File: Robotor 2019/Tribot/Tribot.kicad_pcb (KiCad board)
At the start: 2 copper layers, 95.2 x 95.2 mm, 74 parts, among them J1 Conn_01x03_Male, J2 Conn_01x04_Female, J3 USB_B_Mini, J4 Conn_01x04_Female, J5 Conn_01x04_Female, J6 Conn_01x04_Female, J7 Conn_01x03_Female, J8 Conn_01x03_Female, M1 Motor_DC, M2 Motor_DC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

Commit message: The PCB for Tribot up to the point we realised we need a 2nd floor.
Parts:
- removed J4: Conn_01x04_Female, Connector_PinHeader_2.54mm:PinHeader_1x04_P2.54mm_Vertical
- removed the R8 at (139.3, 20.0)
- removed the R8 at (136.6, 82.4)
- added R8: 10K, Resistor_SMD:R_0805_2012Metric_Pad1.15x1.40mm_HandSolder, F.Cu at (228.8, 101.6)
- C4, C5, C6, C7, J3, R10, R11, R3, R9, Y1, Y2: moved to B.Cu
- moved J3 166.6 mm to (263.5, 85.7), turned to 270 degrees
- moved J2 161.8 mm to (237.5, 125.7), turned to 0 degrees
- moved C3 150.6 mm to (38.3, 156.2)
- moved J8 142.1 mm to (251.8, 126.4)
- moved J7 142.1 mm to (256.5, 126.4)
- moved Y2 133.6 mm to (215.4, 66.0), turned to 180 degrees
- moved Y1 128.2 mm to (233.2, 66.0)
- moved R7 128.0 mm to (261.9, 128.3)
- moved JP2 127.3 mm to (229.9, 105.4), turned to 270 degrees
- moved R5 122.8 mm to (246.6, 128.3)
- moved C8 122.4 mm to (38.3, 162.6)
- moved JP1 122.3 mm to (227.3, 109.2), turned to 90 degrees
- moved R11 121.2 mm to (253.0, 89.5)
- moved CP5 113.7 mm to (61.7, 179.1)
- moved C5 112.9 mm to (227.1, 71.1), turned to 180 degrees
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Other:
- outline, holes or cut-outs redrawn

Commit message: Bottom tribot circuit board.
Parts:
- removed C12: 100n, Capacitor_SMD:C_0805_2012Metric_Pad1.15x1.40mm_HandSolder
- removed CP1: 1uF, Capacitor_SMD:CP_Elec_4x5.3
- removed J6: Conn_01x04_Female, Connector_PinHeader_2.54mm:PinHeader_1x04_P2.54mm_Vertical
- removed U2: AMS1117-3V3, Package_TO_SOT_SMD:SOT-223-3_TabPin2
- added BOOT_PIN1: Conn_01x02, Connector_PinHeader_2.54mm:PinHeader_1x02_P2.54mm_Vertical, F.Cu at (199.9, 52.1)
- added BOOT_PIN2: Conn_01x02, Connector_PinHeader_2.54mm:PinHeader_1x02_P2.54mm_Vertical, F.Cu at (73.4, 117.3)
- added J4: Conn_01x04_Female, Connector_PinHeader_2.54mm:PinHeader_1x04_P2.54mm_Vertical, F.Cu at (52.1, 60.3)
- added M_PIN1: Conn_01x03, Connector_PinSocket_2.54mm:PinSocket_1x03_P2.54mm_Vertical, F.Cu at (111.5, 143.6)
- added M_PIN2: Conn_01x03, Connector_PinSocket_2.54mm:PinSocket_1x03_P2.54mm_Vertical, F.Cu at (238.0, 80.8)
- added M_PIN3: Conn_01x03, Connector_PinSocket_2.54mm:PinSocket_1x03_P2.54mm_Vertical, F.Cu at (116.8, 143.5)
- added M_PIN4: Conn_01x03, Connector_PinSocket_2.54mm:PinSocket_1x03_P2.54mm_Vertical, F.Cu at (243.3, 80.8)
- added PRGRM_PIN1: Conn_01x02, Connector_PinHeader_2.54mm:PinHeader_1x02_P2.54mm_Vertical, F.Cu at (192.8, 39.9)
- added PRGRM_PIN2: Conn_01x02, Connector_PinHeader_2.54mm:PinHeader_1x02_P2.54mm_Vertical, F.Cu at (66.3, 102.6)
- added USB_PIN1: Conn_01x02, Connector_PinHeader_2.54mm:PinHeader_1x02_P2.54mm_Vertical, F.Cu at (68.8, 107.7)
- added USB_PIN2: Conn_01x02, Connector_PinHeader_2.54mm:PinHeader_1x02_P2.54mm_Vertical, F.Cu at (195.3, 45.0)
- added US_PIN1: Conn_01x02, Connector_PinHeader_2.54mm:PinHeader_1x02_P2.54mm_Vertical, F.Cu at (69.6, 122.9)
- added US_PIN2: Conn_01x02, Connector_PinHeader_2.54mm:PinHeader_1x02_P2.54mm_Vertical, F.Cu at (196.1, 60.2)
- added US_PIN3: Conn_01x02, Connector_PinHeader_2.54mm:PinHeader_1x02_P2.54mm_Vertical, F.Cu at (196.1, 52.1)
- added US_PIN4: Conn_01x02, Connector_PinHeader_2.54mm:PinHeader_1x02_P2.54mm_Vertical, F.Cu at (69.6, 114.8)
- added V_PIN1: Conn_01x02, Connector_Wire:SolderWirePad_1x02_P5.08mm_Drill1.5mm, F.Cu at (66.5, 148.6)
- added V_PIN2: Conn_01x03, Connector_Wire:SolderWirePad_1x03_P5.715mm_Drill2mm, F.Cu at (48.5, 37.3)
- added V_PIN2: Conn_01x02, Connector_Wire:SolderWirePad_1x02_P5.08mm_Drill1.5mm, F.Cu at (193.0, 85.9)
- D1, D2, D3, D4, D5, D6, D7, D8: footprint Diode_THT:D_DO-15_P5.08mm_Vertical_AnodeUp -> Diode_THT:D_A-405_P5.08mm_Vertical_AnodeUp
- J3, R10, R11, R3, R9: moved to F.Cu
- moved J2 200.9 mm to (47.5, 60.3)
- moved J7 185.7 mm to (93.7, 37.0)
- moved R2 182.9 mm to (46.0, 135.9), turned to 90 degrees
- moved U4 179.3 mm to (52.1, 128.3), turned to 90 degrees
- moved J8 176.7 mm to (100.3, 35.3)
- moved C1 169.8 mm to (46.7, 145.3)
- moved R1 168.1 mm to (46.7, 142.7)
- moved CP6 168.0 mm to (82.5, 13.7), turned to 270 degrees
- moved R7 167.6 mm to (107.3, 63.6)
- moved CP4 166.6 mm to (53.3, 148.6)
- moved C8 163.8 mm to (82.5, 4.83), turned to 90 degrees
- moved R5 162.9 mm to (94.4, 70.4)
- moved R6 161.7 mm to (53.3, 144.8), turned to 180 degrees
- moved U5 161.6 mm to (58.4, 158.8)
- moved R12 161.5 mm to (58.4, 166.4)
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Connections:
- C15 pad 1: +5V -> 5V
- C17 pad 1: +5V -> 5V
- C18 pad 1: +5V -> 5V
- C21 pad 1: +5V -> 5V
- C8 pad 1: +7.5V -> EXT_VCC
- CP2 pad 1: +7.5V -> EXT_VCC
- CP3 pad 1: +7.5V -> EXT_VCC
- CP4 pad 1: +3V3 -> 3V3
- CP6 pad 1: +7.5V -> EXT_VCC
- D1 pad 1: +7.5V -> EXT_VCC
- D3 pad 1: +7.5V -> EXT_VCC
- D5 pad 1: +7.5V -> EXT_VCC
- D7 pad 1: +7.5V -> EXT_VCC
- J1 pad 1: +7.5V -> EXT_VCC
- J7 pad 3: +3V3 -> 3V3
- J8 pad 3: +3V3 -> 3V3
- R1 pad 1: +3V3 -> 3V3
- R10 pad 1: PA12 -> USB++
- R12 pad 1: +5V -> 5V
- R14 pad 1: +5V -> 5V
- R16 pad 1: +5V -> 5V
- R18 pad 1: +5V -> 5V
- R2 pad 1: +3V3 -> 3V3
- R5 pad 1: +3V3 -> 3V3
- R6 pad 1: +3V3 -> 3V3
- R7 pad 1: +3V3 -> 3V3
- R9 pad 2: PA11 -> USB--
- U1 pad 3: +7.5V -> EXT_VCC
- U3 pad 3: +7.5V -> EXT_VCC
- U4 pad 18: EnA -> EnA_B
- U4 pad 19: EnB -> EnB_B
- U4 pad 20: BOOT1 -> BOOT1_B
- U4 pad 24: +3V3 -> 3V3
- U4 pad 25: US1_IN -> US1P_IN
- U4 pad 26: US1_OUT -> US1P_OUT
- U4 pad 27: US2_IN -> US2P_IN
- U4 pad 28: US2_OUT -> US2P_OUT
- U4 pad 32: PA11 -> USB-
- U4 pad 33: PA12 -> USB+
- U4 pad 34: DIO -> DIO_B
- U4 pad 36: +3V3 -> 3V3
- U4 pad 37: CLK -> CLK_B
- U4 pad 38: M2IN2 -> M2IN2_B
- U4 pad 39: M2IN1 -> M2IN1_B
- U4 pad 40: M1IN2 -> M1IN2_B
- U4 pad 41: M1IN1 -> M1IN1_B
- U4 pad 44: BOOT0 -> BOOT0_B
- U4 pad 45: US3_IN -> Net-(U4-Pad45)
- U4 pad 46: US3_OUT -> Net-(U4-Pad46)
- U4 pad 48: +3V3 -> 3V3
- U6 pad 6: +7.5V -> EXT_VCC
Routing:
- net M2IN1_B: track 0.00 -> 131.5 mm
- net M2IN2_B: track 0.00 -> 129.9 mm
- net OSC32-IN: track 0.00 -> 118.9 mm, vias 0 -> 1
- net M1IN2_B: track 0.00 -> 118.1 mm
- net M1IN1_B: track 0.00 -> 113.6 mm
- net 5V: track 0.00 -> 104.7 mm, vias 0 -> 1
- net OSC-OUT: track 0.00 -> 90.3 mm, vias 0 -> 1
- net OSC32-OUT: track 0.00 -> 86.5 mm, vias 0 -> 1
- net 3V3: track 0.00 -> 81.3 mm, vias 0 -> 3
- net OSC-IN: track 0.00 -> 74.6 mm, vias 0 -> 1
- net EnB_B: track 0.00 -> 70.3 mm
- net EnA_B: track 0.00 -> 66.6 mm
- net BOOT0_B: track 0.00 -> 46.6 mm, vias 0 -> 1
- net CLK_B: track 0.00 -> 34.4 mm
- net DIO_B: track 0.00 -> 33.9 mm
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- added copper zone on B.Cu, net GND
- added copper zone on F.Cu, net GND
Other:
- board size 95.2 x 95.2 mm -> 220.5 x 156.7 mm

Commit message: Tribot bottom circuit board final version (hopefully)
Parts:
- added D10: DIODE, Diode_THT:D_A-405_P5.08mm_Vertical_AnodeUp, F.Cu at (62.0, 48.3)
- added REF**: MountingHole_2.5mm, MountingHole:MountingHole_2.5mm, F.Cu at (127.5, 130.6)
- added REF**: MountingHole_2.5mm, MountingHole:MountingHole_2.5mm, F.Cu at (127.5, 145.5)
- added REF**: MountingHole_2.5mm, MountingHole:MountingHole_2.5mm, F.Cu at (45.7, 145.8)
- added REF**: MountingHole_2.5mm, MountingHole:MountingHole_2.5mm, F.Cu at (45.7, 130.8)
- moved C5 12.4 mm to (119.1, 144.8)
- moved C6 12.4 mm to (109.5, 144.8)
- moved C7 12.4 mm to (109.0, 124.5)
- moved Y1 12.4 mm to (119.1, 134.6)
- moved Y2 12.4 mm to (110.5, 134.6)
- moved C4 11.7 mm to (117.1, 123.2), turned to 90 degrees
- moved M_PIN3 10.9 mm to (122.7, 152.7)
- moved M_PIN2 10.9 mm to (243.8, 89.9)
- moved M_PIN4 10.9 mm to (249.2, 89.9)
- moved M_PIN1 10.9 mm to (117.3, 152.7)
- moved R15 8.38 mm to (66.8, 144.8)
- moved U7 7.94 mm to (59.9, 145.0)
- moved R14 7.94 mm to (59.9, 152.7)
- moved C17 7.94 mm to (66.3, 148.8)
- moved C18 7.58 mm to (65.8, 134.1)
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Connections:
- C8 pad 1: EXT_VCC -> +7.5V
- CP2 pad 1: EXT_VCC -> +7.5V
- CP3 pad 1: EXT_VCC -> +7.5V
- CP6 pad 1: EXT_VCC -> +7.5V
- D1 pad 1: EXT_VCC -> +7.5V
- D3 pad 1: EXT_VCC -> +7.5V
- D5 pad 1: EXT_VCC -> +7.5V
- D7 pad 1: EXT_VCC -> +7.5V
- J1 pad 1: EXT_VCC -> +7.5V
- U1 pad 3: EXT_VCC -> +7.5V
- U3 pad 3: EXT_VCC -> +7.5V
- U6 pad 6: EXT_VCC -> +7.5V
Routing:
- net M2IN2_B: track 129.9 -> 155.7 mm
- net M2IN1_B: track 131.5 -> 155.6 mm
- net M1IN2_B: track 118.1 -> 139.7 mm
- net M1IN1_B: track 113.6 -> 135.1 mm
- net 5V: track 104.7 -> 87.9 mm
- net OSC-OUT: track 90.3 -> 75.2 mm
- net EnB_B: track 70.3 -> 82.4 mm
- net EnA_B: track 66.6 -> 75.5 mm
- net 3V3: track 81.3 -> 90.2 mm
- net OSC32-OUT: track 86.5 -> 93.9 mm
- net BOOT0_B: track 46.6 -> 51.9 mm
- net OSC-IN: track 74.6 -> 78.9 mm
- net US2P_OUT: track 23.8 -> 20.2 mm
- net US2P_IN: track 20.6 -> 17.3 mm
- net S3: track 11.4 -> 8.52 mm
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
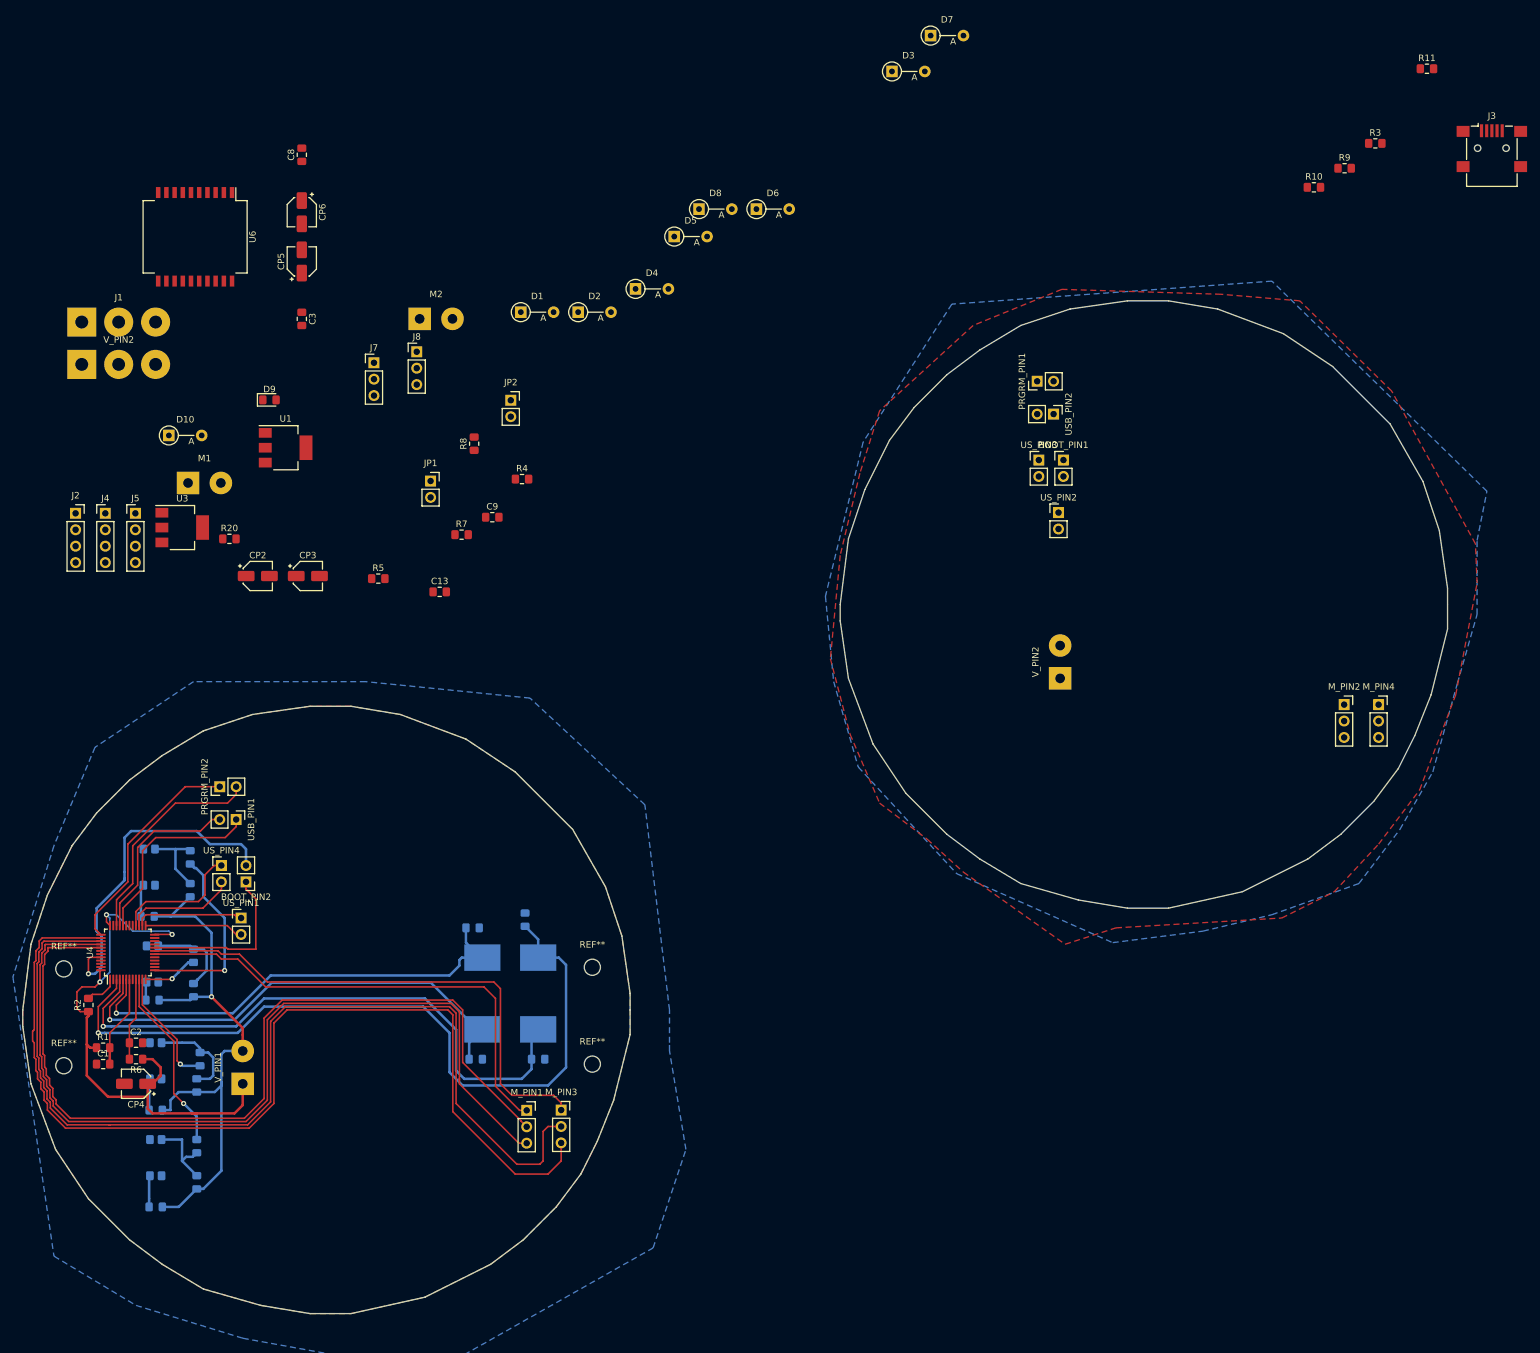
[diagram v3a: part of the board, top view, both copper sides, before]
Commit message: Small tweaks to vias, paths, added parts lists.
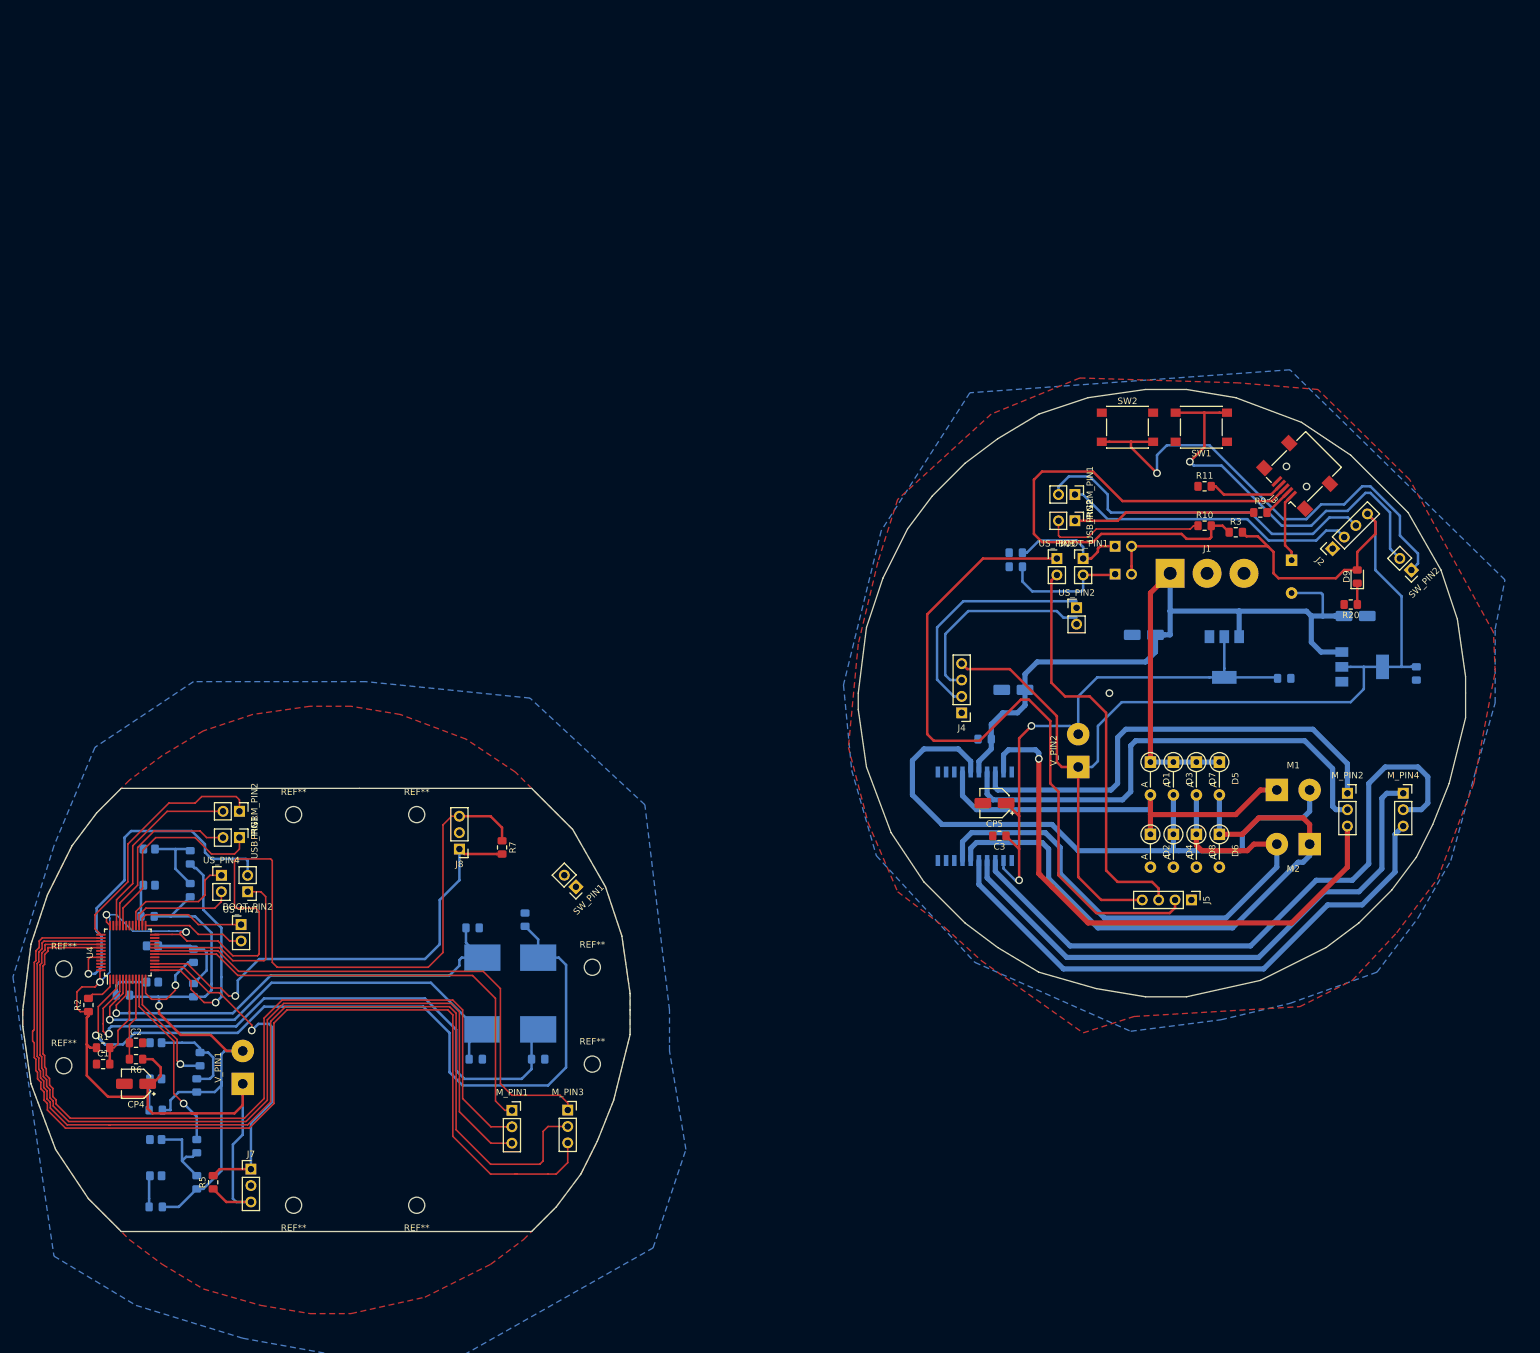
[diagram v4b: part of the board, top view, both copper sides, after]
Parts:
- removed the V_PIN2 at (48.5, 37.3)
- removed the V_PIN2 at (199.9, 85.9)
- added REF**: MountingHole_2.5mm, MountingHole:MountingHole_2.5mm, F.Cu at (100.3, 167.4)
- added REF**: MountingHole_2.5mm, MountingHole:MountingHole_2.5mm, F.Cu at (81.3, 167.4)
- added REF**: MountingHole_2.5mm, MountingHole:MountingHole_2.5mm, F.Cu at (81.3, 106.9)
- added REF**: MountingHole_2.5mm, MountingHole:MountingHole_2.5mm, F.Cu at (100.3, 106.9)
- added SW1: SW_Push, Button_Switch_SMD:SW_Push_1P1T_NO_6x6mm_H9.5mm, F.Cu at (221.7, 47.0)
- added SW2: SW_Push, Button_Switch_SMD:SW_Push_1P1T_NO_6x6mm_H9.5mm, F.Cu at (210.3, 47.0)
- added SW_PIN1: Conn_01x02, Connector_PinSocket_2.54mm:PinSocket_1x02_P2.54mm_Vertical, F.Cu at (125.0, 118.1)
- added SW_PIN2: Conn_01x02, Connector_PinSocket_2.54mm:PinSocket_1x02_P2.54mm_Vertical, F.Cu at (254.3, 69.1)
- added V_PIN2: Conn_01x02, Connector_Wire:SolderWirePad_1x02_P5.08mm_Drill1.5mm, F.Cu at (202.7, 99.6)
- C13, C8, C9, CP2, CP3, CP6, JP1, JP2, R4, R8, U1, U3, U6: moved to B.Cu
- D10: value DIODE -> D; moved to B.Cu
- moved J2 194.6 mm to (242.1, 65.8), turned to 135 degrees
- moved M1 175.1 mm to (233.4, 103.1)
- moved D10 174.8 mm to (235.7, 67.6), turned to 270 degrees
- moved J5 174.0 mm to (220.2, 120.1), turned to 270 degrees
- moved R20 173.8 mm to (244.9, 74.4), turned to 180 degrees
- moved J1 172.9 mm to (216.9, 69.6)
- moved D9 170.5 mm to (245.9, 70.1), turned to 90 degrees
- moved U1 170.0 mm to (246.6, 84.1)
- moved CP2 170.0 mm to (245.6, 76.2)
- moved U3 162.5 mm to (225.3, 82.5), turned to 270 degrees
- moved M2 159.9 mm to (238.5, 111.5), turned to 180 degrees
- moved U6 150.3 mm to (186.7, 107.2)
- moved C9 145.0 mm to (255.0, 85.1), turned to 270 degrees
- moved C8 139.1 mm to (188.2, 95.2), turned to 180 degrees
- moved CP5 136.1 mm to (189.7, 105.2), turned to 180 degrees
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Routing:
- net +3V3: track 0.00 -> 209.5 mm
- net 3V3: track 90.2 -> 236.0 mm
- net +7.5V: track 0.00 -> 145.4 mm
- net US2_OUT: track 0.00 -> 112.1 mm
- net M2IN1: track 0.00 -> 101.1 mm
- net Net-(D3-Pad2): track 0.00 -> 98.4 mm
- net Net-(D5-Pad2): track 0.00 -> 93.9 mm
- net EnB: track 0.00 -> 89.1 mm
- net M1IN2: track 0.00 -> 88.2 mm, vias 0 -> 1
- net Net-(D7-Pad2): track 0.00 -> 87.8 mm
- net M2IN2: track 0.00 -> 87.3 mm
- net +5V: track 0.00 -> 86.8 mm, vias 0 -> 2
- net Net-(J3-Pad3): track 0.00 -> 84.2 mm
- net M1IN1: track 0.00 -> 75.3 mm
- net Net-(SW2-Pad2): track 0.00 -> 74.2 mm, vias 0 -> 1
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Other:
- board size 220.5 x 156.7 mm -> 223.3 x 130.3 mm
- net class +7.5V added: clearance 0.4, trace_width 0.8, via_dia 1.2, via_drill 0.8
- net class Default: via_dia 0.8 -> 1.2; via_drill 0.4 -> 0.8
